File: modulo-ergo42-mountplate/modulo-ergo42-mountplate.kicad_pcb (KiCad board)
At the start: 2 copper layers, 137.2 x 80 mm, 52 parts, among them J1 AudioJack4_Ground, J2 AudioJack4_Ground, J3 AudioJack4_Ground, J4 AudioJack4_Ground, SW1 SW_Push, SW10 SW_Push, SW11 SW_Push, SW12 SW_Push, SW13 SW_Push, SW14 SW_Push, SW15 SW_Push, SW16 SW_Push, SW17 SW_Push, SW18 SW_Push, SW19 SW_Push, SW2 SW_Push, SW20 SW_Push, SW21 SW_Push, SW22 SW_Push, SW23 SW_Push, SW24 SW_Push, SW25 SW_Push, SW26 SW_Push, SW27 SW_Push, SW28 SW_Push, SW29 SW_DIP_x02, SW3 SW_Push, SW4 SW_Push, SW5 SW_Push, SW6 SW_Push, SW7 SW_Push, SW8 SW_Push, SW9 SW_Push, U1 TCA9555PWR, U2 TCA9555PWR

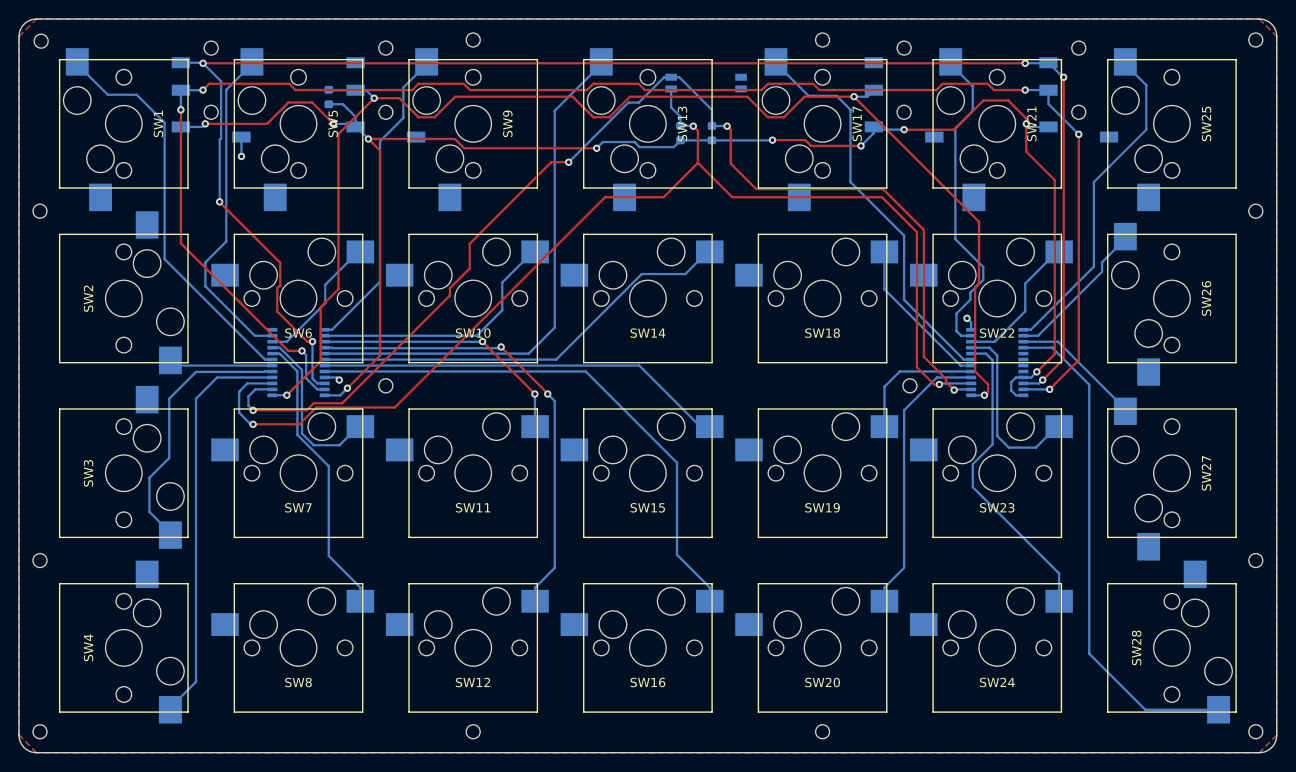
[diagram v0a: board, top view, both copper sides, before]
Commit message: Place MX hole
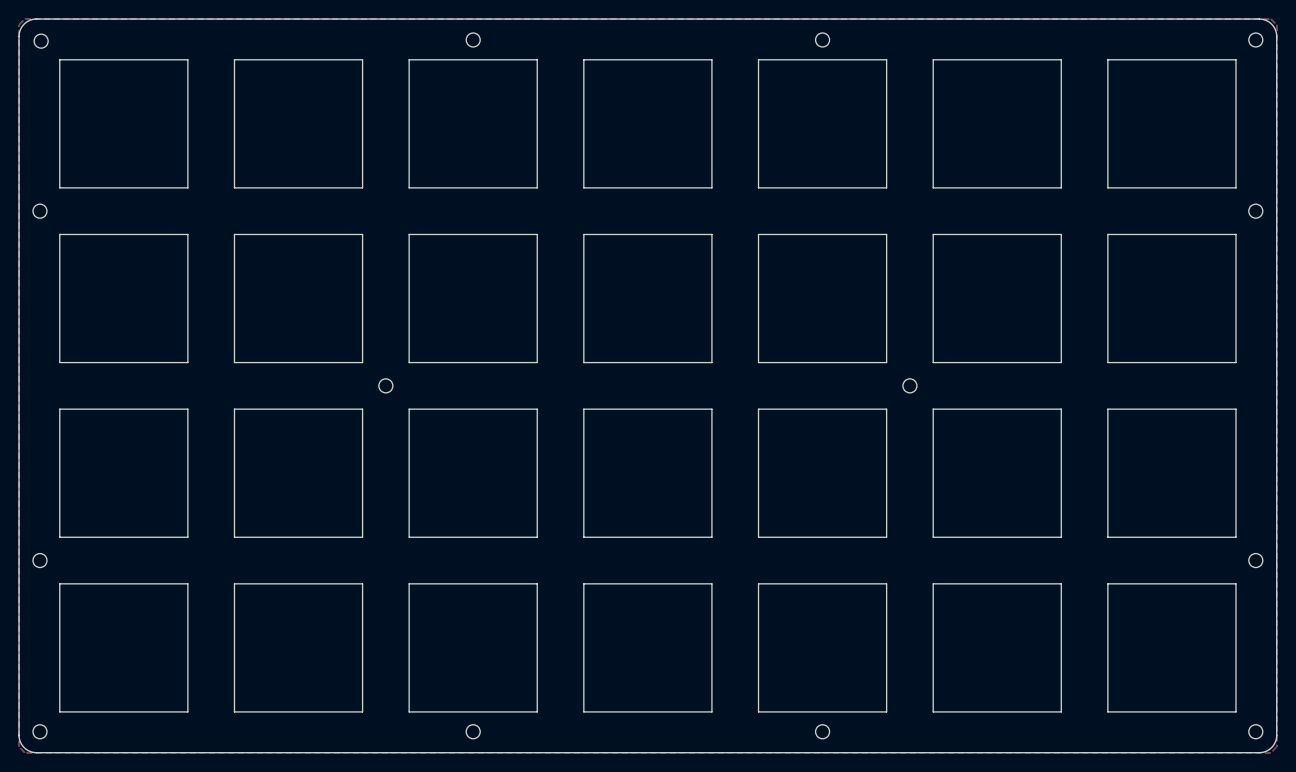
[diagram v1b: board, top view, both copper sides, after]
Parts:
- removed J1, J2, J3, J4: AudioJack4_Ground, library:TRRS_SMD_PJ320
- removed R1, R2, R3: 10 kΩ, Resistor_SMD:R_0603_1608Metric
- removed SW1, SW10, SW11, SW12, SW13, SW14, SW15, SW16, SW17, SW18, SW19, SW2, SW20, SW21, SW22, SW23, SW24, SW25, SW26, SW27, SW28, SW3, SW4, SW5, SW6, SW7, SW8, SW9: SW_Push, library:Kailh_Socket
- removed SW29: SW_DIP_x02, library:DipSwitch
- removed U1, U2: TCA9555PWR, Package_SO:TSSOP-24_4.4x7.8mm_P0.65mm
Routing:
- net SDA: track 176.1 -> 0.00 mm, vias 6 -> 0
- net SCL: track 174.8 -> 0.00 mm, vias 6 -> 0
- net 3V3: track 174.5 -> 0.00 mm, vias 10 -> 0
- net INT: track 144.1 -> 0.00 mm, vias 4 -> 0
- net A2: track 127.2 -> 0.00 mm, vias 3 -> 0
- net A1: track 125.7 -> 0.00 mm, vias 4 -> 0
- net R4C4: track 59.1 -> 0.00 mm
- net R1C4: track 57.3 -> 0.00 mm
- net R4C7: track 54.8 -> 0.00 mm
- net R4C3: track 50.4 -> 0.00 mm, vias 2 -> 0
- net R2C4: track 46.9 -> 0.00 mm
- net R3C4: track 44.8 -> 0.00 mm
- net R4C1: track 44.4 -> 0.00 mm
- net R1C5: track 43.8 -> 0.00 mm
- net R1C1: track 43.6 -> 0.00 mm
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- added copper zone on B.Cu, net (none)
- added copper zone on F.Cu, net (none)
- removed copper zone on B.Cu, net GND
- removed copper zone on F.Cu, net GND
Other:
- outline, holes or cut-outs redrawn

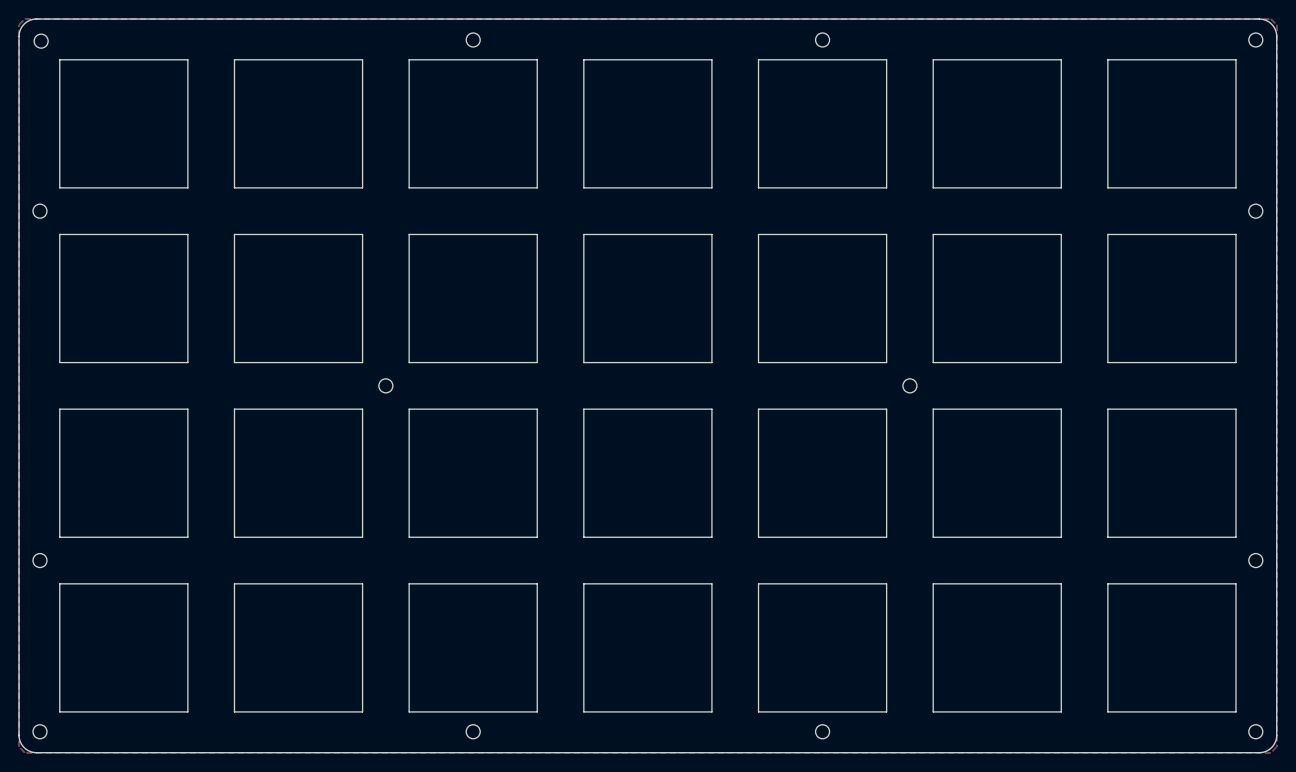
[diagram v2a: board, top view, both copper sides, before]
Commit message: Fix mount plate screw hole
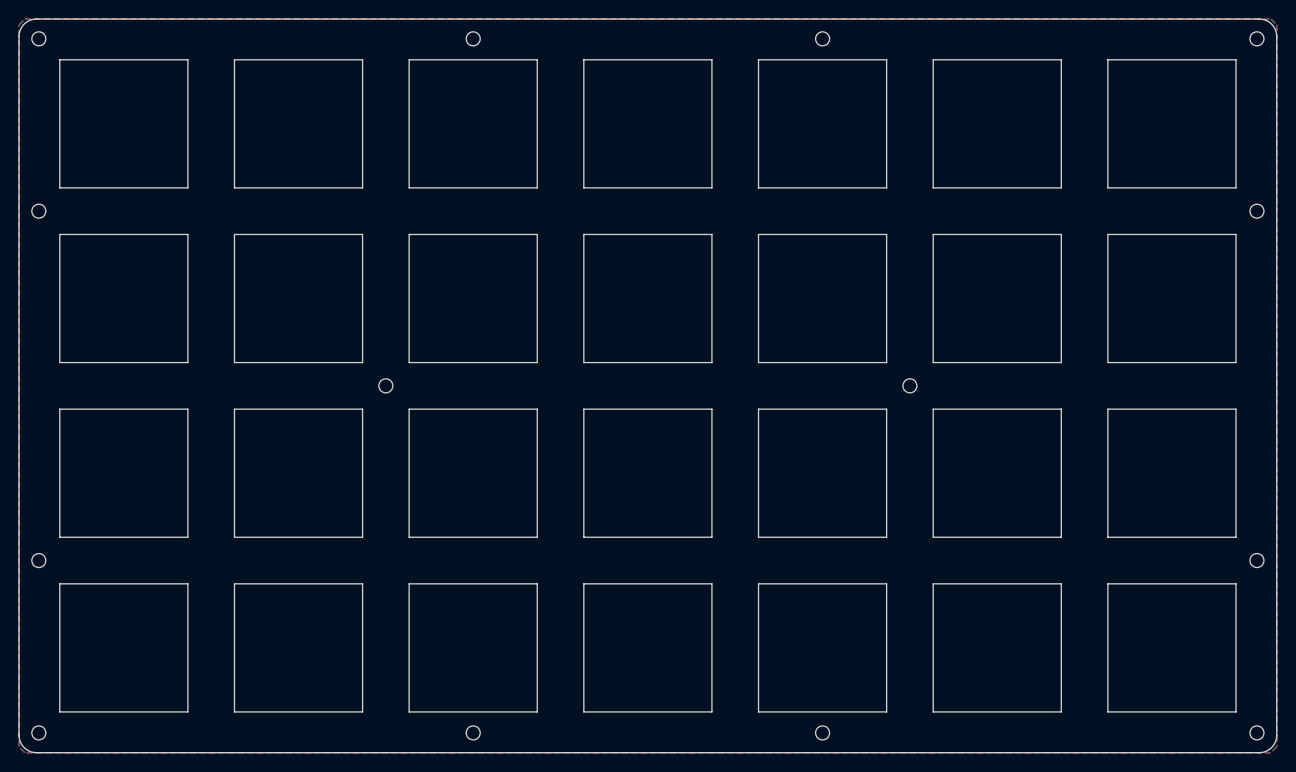
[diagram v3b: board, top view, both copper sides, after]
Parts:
- removed the ? at (56.9, 55.2)
- removed the ? at (142.2, 112.0)
- removed the ? at (189.5, 112.0)
- removed the ? at (189.5, 36.6)
- removed the ? at (56.9, 93.3)
- removed the ? at (189.5, 93.3)
- removed the ? at (189.5, 55.2)
- removed the ? at (142.2, 36.6)
- removed the ? at (56.9, 112.0)
- removed the ? at (104.1, 112.0)
- added ?: Screw_Hole, library:Screw_Hole, F.Cu at (56.8, 55.2)
- added ?: Screw_Hole, library:Screw_Hole, F.Cu at (142.2, 112.1)
- added ?: Screw_Hole, library:Screw_Hole, F.Cu at (189.6, 112.1)
- added ?: Screw_Hole, library:Screw_Hole, F.Cu at (189.6, 36.4)
- added ?: Screw_Hole, library:Screw_Hole, F.Cu at (56.8, 93.3)
- added ?: Screw_Hole, library:Screw_Hole, F.Cu at (189.6, 93.3)
- added ?: Screw_Hole, library:Screw_Hole, F.Cu at (189.6, 55.2)
- added ?: Screw_Hole, library:Screw_Hole, F.Cu at (142.2, 36.4)
- added ?: Screw_Hole, library:Screw_Hole, F.Cu at (56.8, 112.1)
- added ?: Screw_Hole, library:Screw_Hole, F.Cu at (104.1, 112.1)
- moved ? 0.36 mm to (56.8, 36.4)
- moved ? 0.13 mm to (104.1, 36.4)
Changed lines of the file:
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@@
   )
   (module library:Screw_Hole (layer F.Cu)
-    (at 56.896 55.245)
+    (at 56.769 55.245)
     (fp_text reference "" (at 0 1.905) (layer F.SilkS)
       (effects (font (size 1 1) (thickness 0.15)))
@@
   )
   (module library:Screw_Hole (layer F.Cu)
-    (at 56.896 93.345)
+    (at 56.769 93.345)
     (fp_text reference "" (at 0 1.905) (layer F.SilkS)
       (effects (font (size 1 1) (thickness 0.15)))
@@
   )
   (module library:Screw_Hole (layer F.Cu)
-    (at 189.484 93.345)
+    (at 189.611 93.345)
     (fp_text reference "" (at 0 1.905) (layer F.SilkS)
       (effects (font (size 1 1) (thickness 0.15)))
@@
   )
   (module library:Screw_Hole (layer F.Cu)
-    (at 189.484 55.245)
+    (at 189.611 55.245)
     (fp_text reference "" (at 0 1.905) (layer F.SilkS)
       (effects (font (size 1 1) (thickness 0.15)))
@@
   )
   (module library:Screw_Hole (layer F.Cu)
-    (at 142.24 36.576)
+    (at 142.24 36.449)
     (fp_text reference "" (at 0 1.905) (layer F.SilkS)
       (effects (font (size 1 1) (thickness 0.15)))
@@
   )
   (module library:Screw_Hole (layer F.Cu)
-    (at 104.14 36.576)
+    (at 104.14 36.449)
     (fp_text reference "" (at 0 1.905) (layer F.SilkS)
       (effects (font (size 1 1) (thickness 0.15)))
@@
   )
   (module library:Screw_Hole (layer F.Cu)
-    (at 57.023 36.703)
+    (at 56.769 36.449)
     (fp_text reference "" (at 0 1.905) (layer F.SilkS)
       (effects (font (size 1 1) (thickness 0.15)))
@@
   )
   (module library:Screw_Hole (layer F.Cu)
-    (at 56.896 112.014)
+    (at 56.769 112.141)
     (fp_text reference "" (at 0 1.905) (layer F.SilkS)
       (effects (font (size 1 1) (thickness 0.15)))
@@
   )
   (module library:Screw_Hole (layer F.Cu)
-    (at 104.14 112.014)
+    (at 104.14 112.141)
     (fp_text reference "" (at 0 1.905) (layer F.SilkS)
       (effects (font (size 1 1) (thickness 0.15)))
@@
   )
   (module library:Screw_Hole (layer F.Cu)
-    (at 142.24 112.014)
+    (at 142.24 112.141)
     (fp_text reference "" (at 0 1.905) (layer F.SilkS)
       (effects (font (size 1 1) (thickness 0.15)))
@@
   )
   (module library:Screw_Hole (layer F.Cu)
-    (at 189.484 112.014)
+    (at 189.611 112.141)
     (fp_text reference "" (at 0 1.905) (layer F.SilkS)
       (effects (font (size 1 1) (thickness 0.15)))
@@
   )
   (module library:Screw_Hole (layer F.Cu)
-    (at 189.484 36.576)
+    (at 189.611 36.449)
     (fp_text reference "" (at 0 1.905) (layer F.SilkS)
       (effects (font (size 1 1) (thickness 0.15)))
